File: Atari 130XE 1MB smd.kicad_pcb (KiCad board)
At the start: 2 copper layers, 324 x 204 mm, 368 parts, among them J1 SIO, J10 Mem_on_off, J102 pin, J103 pin, J104 pin, J105 pin, J2 Video, J201 Diagnostic, J202 Diag, J210 Diag, J24 Cartridge, J4 Expansion, J5 Joystick_Port, J50 Test_signal, J500 Basic_sel, J501 TPP_sel, J51 To_GND, J6 Joystick_Port, J7 Power, J8 Keyboard, Q1 2N3904, Q10 PN2222A, Q101 BC849, Q11 PN2222A, Q2 2N3904, Q3 2N3904, Q4 2N3906, Q6 2N3904, SW1 Switch_power_on, U10 DRAM_4464, U100 74LS157, U101 74LS74, U102 74HC02, U103 74HC02, U104 74LS157, U105 74HC74, U17 GTIA, U18 74LS08, U19 LM555, U2 74LS138, U20 4050, U21 74LS74, U22 POKEY, U23 PIA, U24 CD4051B, U25 CD4051B, U3 MMU, U4 27C010, U40 GAL20V8_DIP, U41 74LS157, U42 74LS175, U43 DRAM_1MB_4bit, U44 DRAM_1MB_4bit, U5 27C010, U6 Freddie, U7 Antic, U8 Sally, U9 DRAM_4464, Y1 Crystal, Y2 4,43 MHz

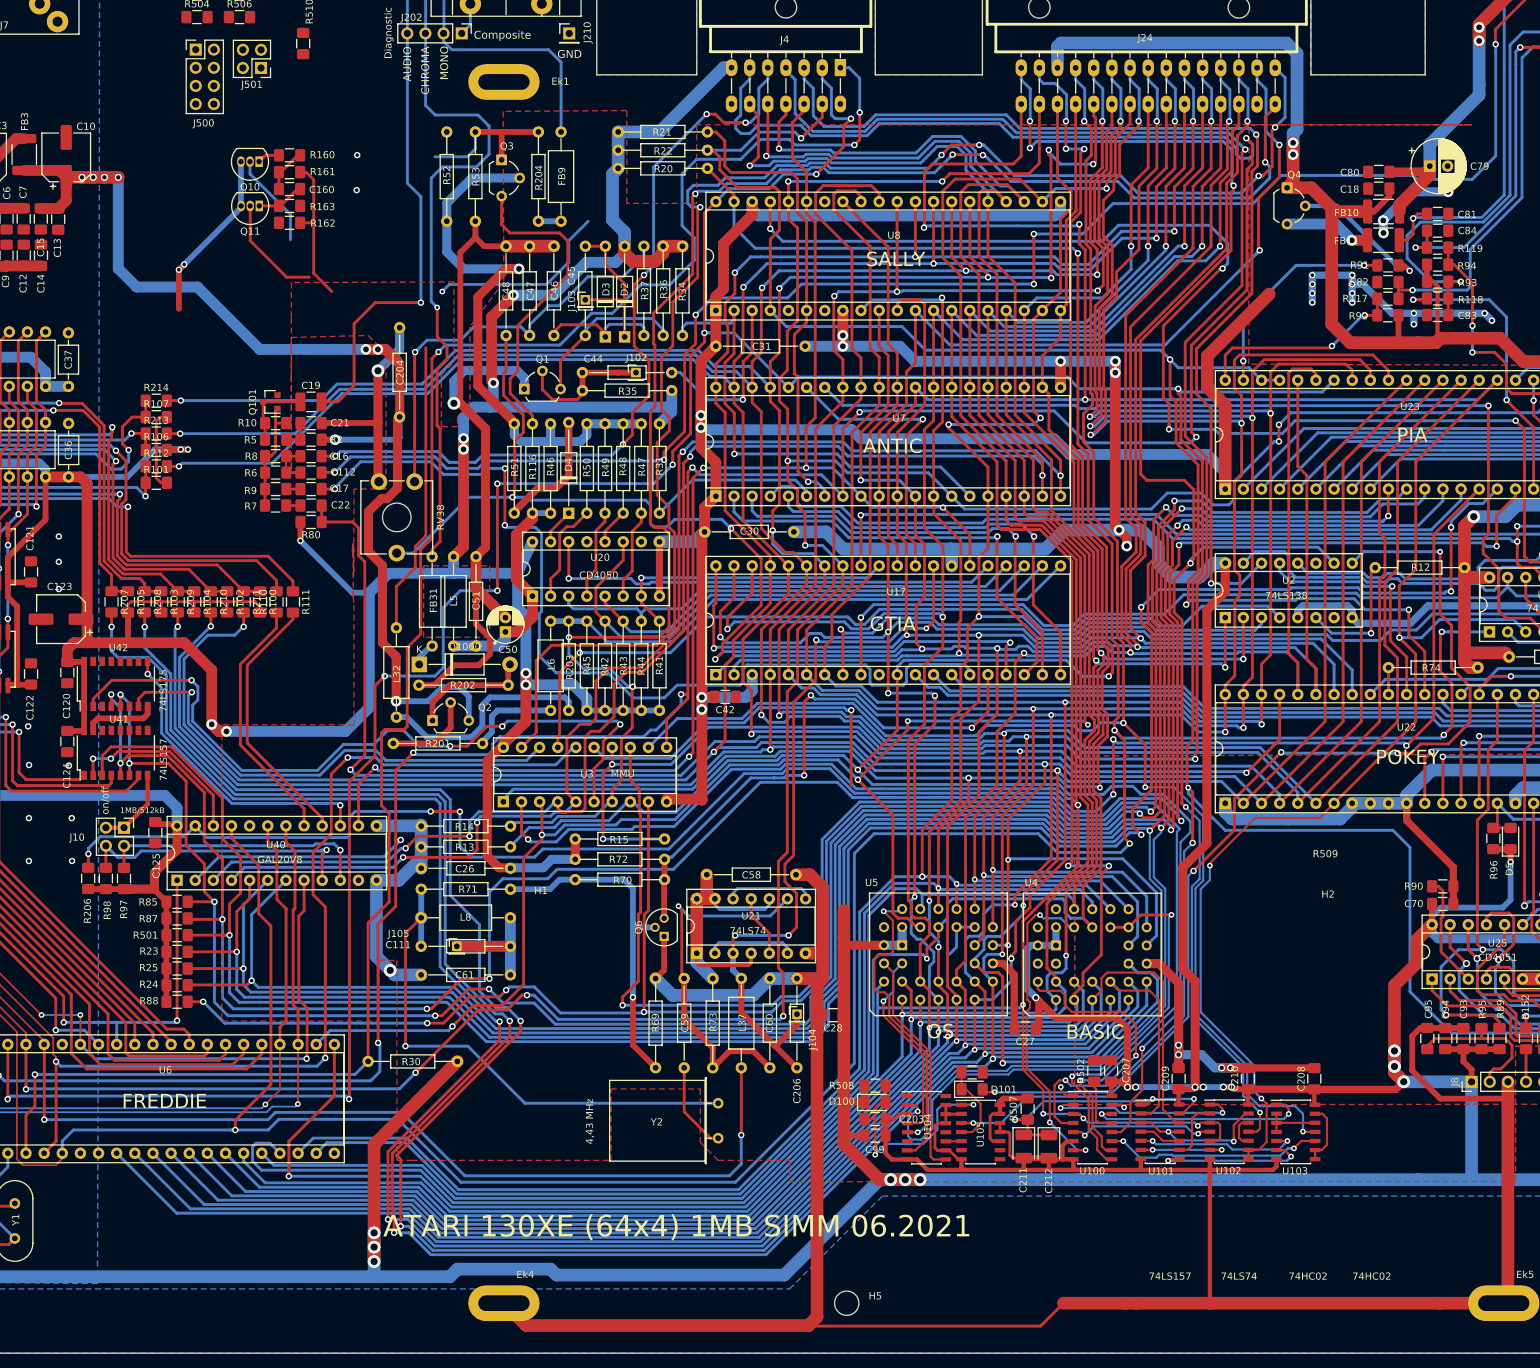
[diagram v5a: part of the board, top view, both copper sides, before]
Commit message: PAL to smd
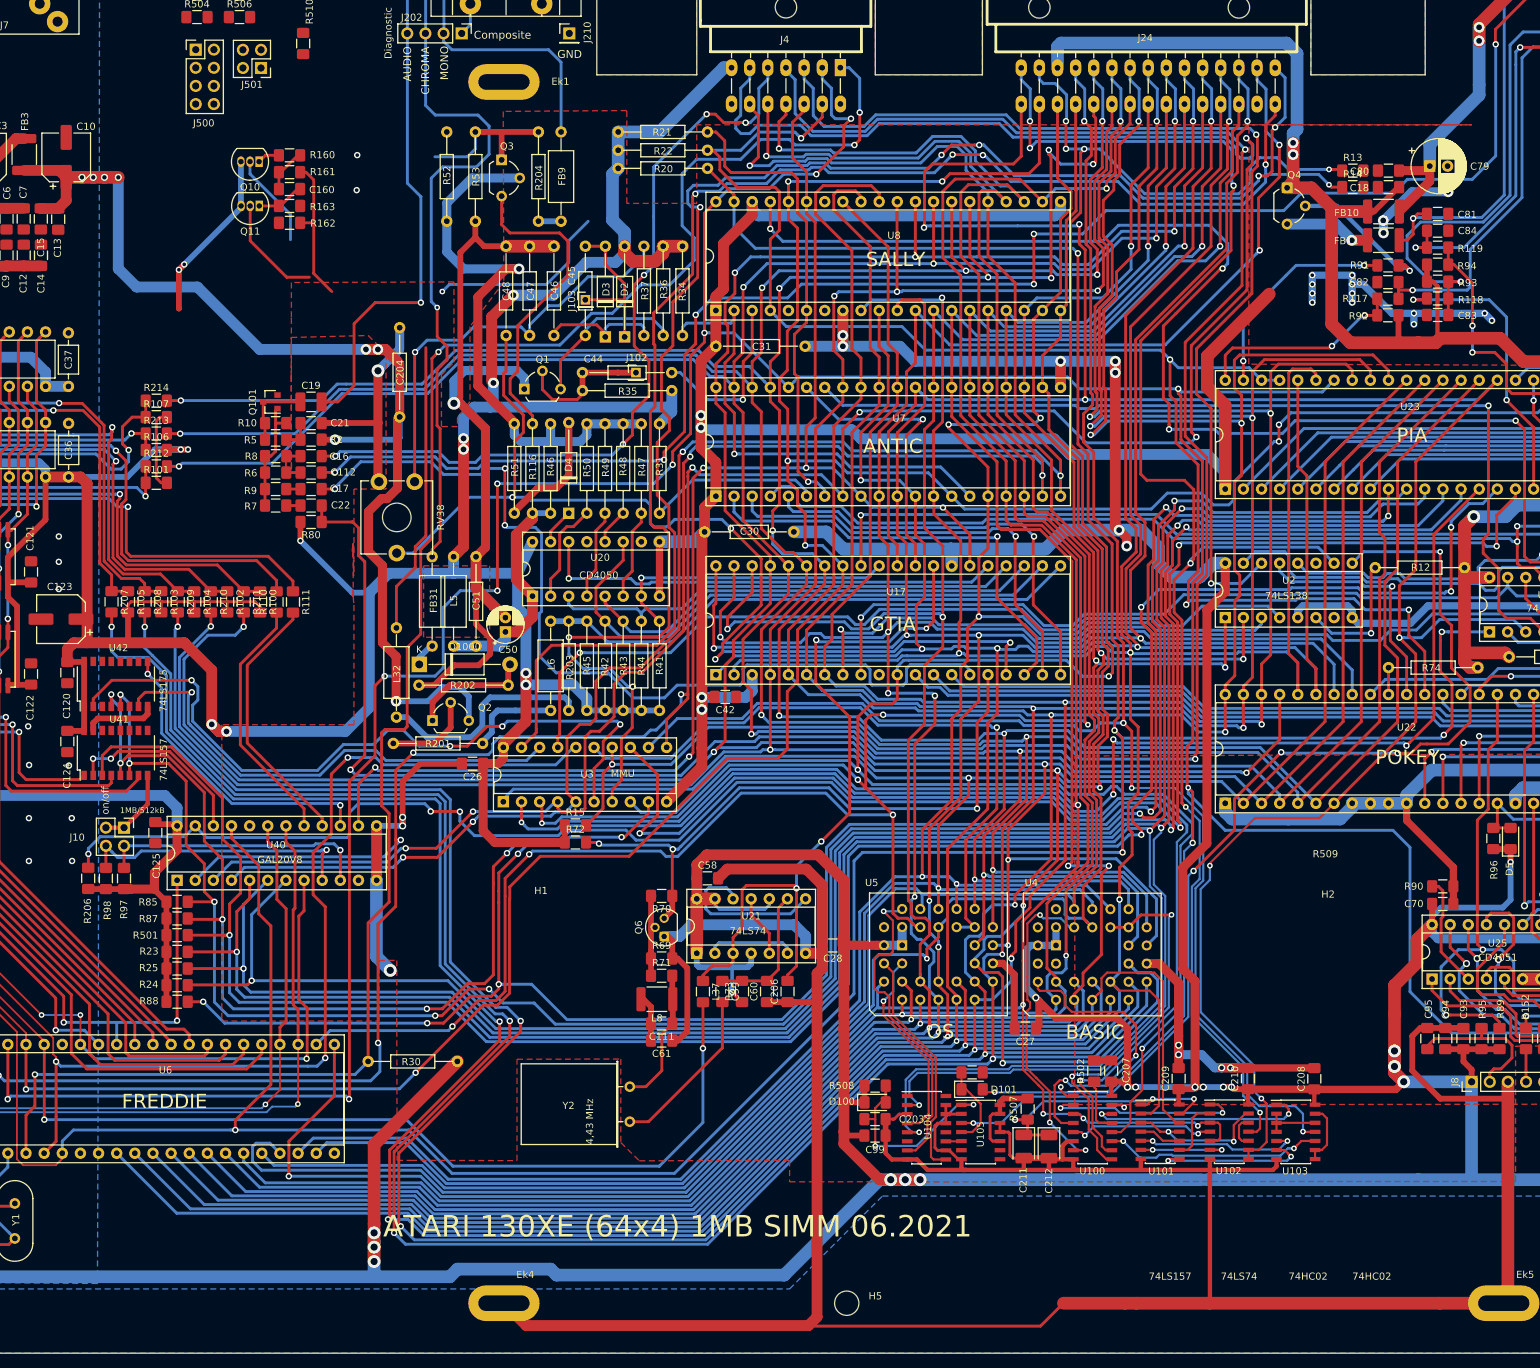
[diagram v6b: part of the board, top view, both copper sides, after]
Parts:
- removed J104, J105: pin, Connector_PinHeader_2.00mm:PinHeader_1x01_P2.00mm_Vertical
- C111, C206, C26, C58, C59, C60, C61: footprint Atari:C_Axial_L5.1mm_D2.5mm_P12.50mm_Horizontal -> Capacitor_SMD:C_1206_3216Metric_Pad1.42x1.75mm_HandSolder
- L37: footprint Atari:L_Axial_L7.0mm_D3.3mm_P12.50mm_Horizontal_Fastron_MICC -> Capacitor_SMD:C_1206_3216Metric_Pad1.42x1.75mm_HandSolder
- L8: footprint Atari:L_Axial_L7.0mm_D3.3mm_P12.50mm_Horizontal_Fastron_MICC -> Inductor_SMD:L_1812_4532Metric_Pad1.30x3.40mm_HandSolder
- R13, R14, R15, R69, R70, R71, R72, R73: footprint Atari:R_Axial_DIN0207_L3.6mm_D2.2mm_P10.16mm_Horizontal -> Resistor_SMD:R_1206_3216Metric_Pad1.42x1.75mm_HandSolder
- moved R13 151.2 mm to (267.7, 81.3), turned to 0 degrees
- moved R14 148.0 mm to (267.7, 83.6), turned to 0 degrees
- moved C111 35.4 mm to (171.0, 200.7), turned to 180 degrees
- moved L8 34.9 mm to (170.3, 197.3), turned to 180 degrees
- moved C61 34.9 mm to (171.0, 203.1), turned to 180 degrees
- moved R71 24.4 mm to (171.0, 194.0), turned to 0 degrees
- moved C26 15.6 mm to (144.5, 164.3)
- moved R69 15.3 mm to (171.0, 191.6), turned to 0 degrees
- moved Y2 12.6 mm to (166.5, 209.6)
- moved C28 9.76 mm to (194.9, 189.8)
- moved L37 5.68 mm to (176.8, 196.2)
- moved C59 5.65 mm to (179.5, 196.2)
- moved R73 4.48 mm to (182.2, 196.2), turned to 90 degrees
- moved R72 2.37 mm to (158.9, 175.4)
- moved R70 2.31 mm to (171.0, 182.8)
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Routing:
- net Net-(C111-Pad1): track 74.0 -> 19.4 mm, vias 1 -> 0
- net A13: track 311.9 -> 365.9 mm, vias 6 -> 8
- net BASIC: track 197.3 -> 155.0 mm
- net OS: track 57.0 -> 93.9 mm
- net Net-(Q6-Pad2): track 47.8 -> 12.1 mm, vias 1 -> 0
- net Net-(C59-Pad1): track 51.4 -> 18.9 mm, vias 1 -> 0
- net GND: track 1664.7 -> 1694.2 mm, vias 71 -> 73
- net +5VA: track 2163.9 -> 2190.1 mm, vias 50 -> 51
- net RD5: track 297.0 -> 321.6 mm, vias 6 -> 7
- net RW: track 507.6 -> 491.4 mm, vias 11 -> 9
- net Net-(Q6-Pad3): track 77.3 -> 89.5 mm
- net O2: track 500.3 -> 488.9 mm
- net PB3: track 346.0 -> 334.8 mm
- net Net-(C59-Pad2): track 12.5 -> 23.7 mm
- net PB0: track 275.5 -> 285.8 mm, vias 7 -> 8
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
